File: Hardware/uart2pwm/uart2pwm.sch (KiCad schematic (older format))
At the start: 43 parts, among them IC1 ATTINY2313A-S, P1 CONN_01X04, P10 LED5, P11 CONN_01X03, P2 CONN_02X03, P3 LED0, P4 LED3, P5 FAN0, P6 LED1, P7 LED4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

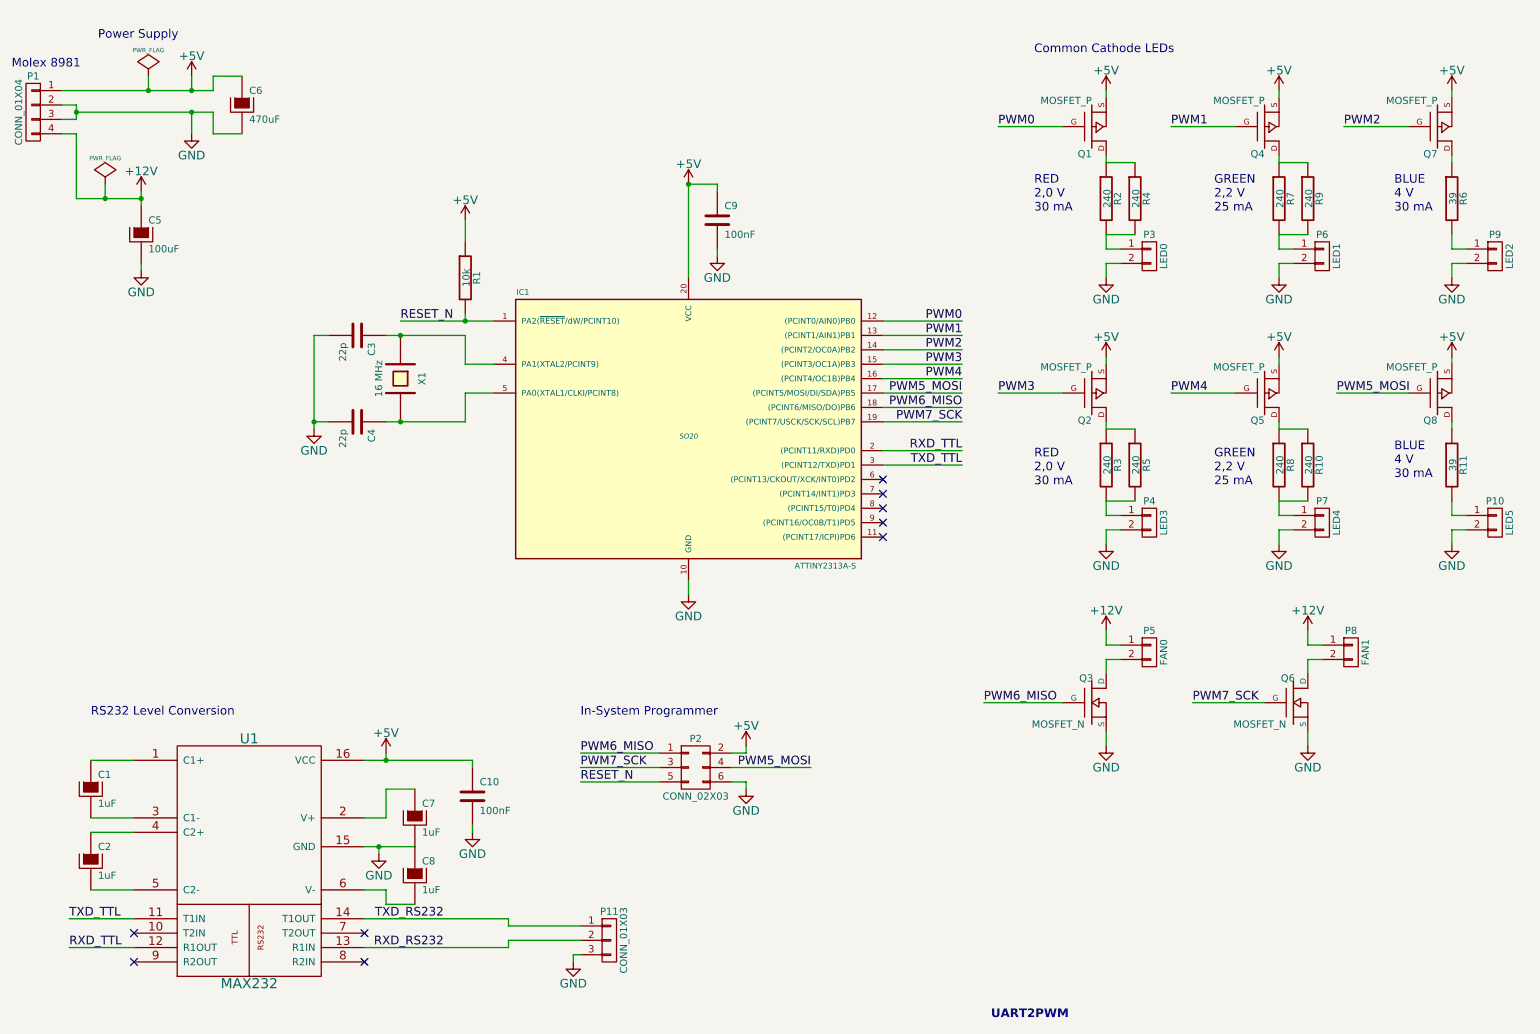
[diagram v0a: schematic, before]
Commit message: Schematic complete; Placement started
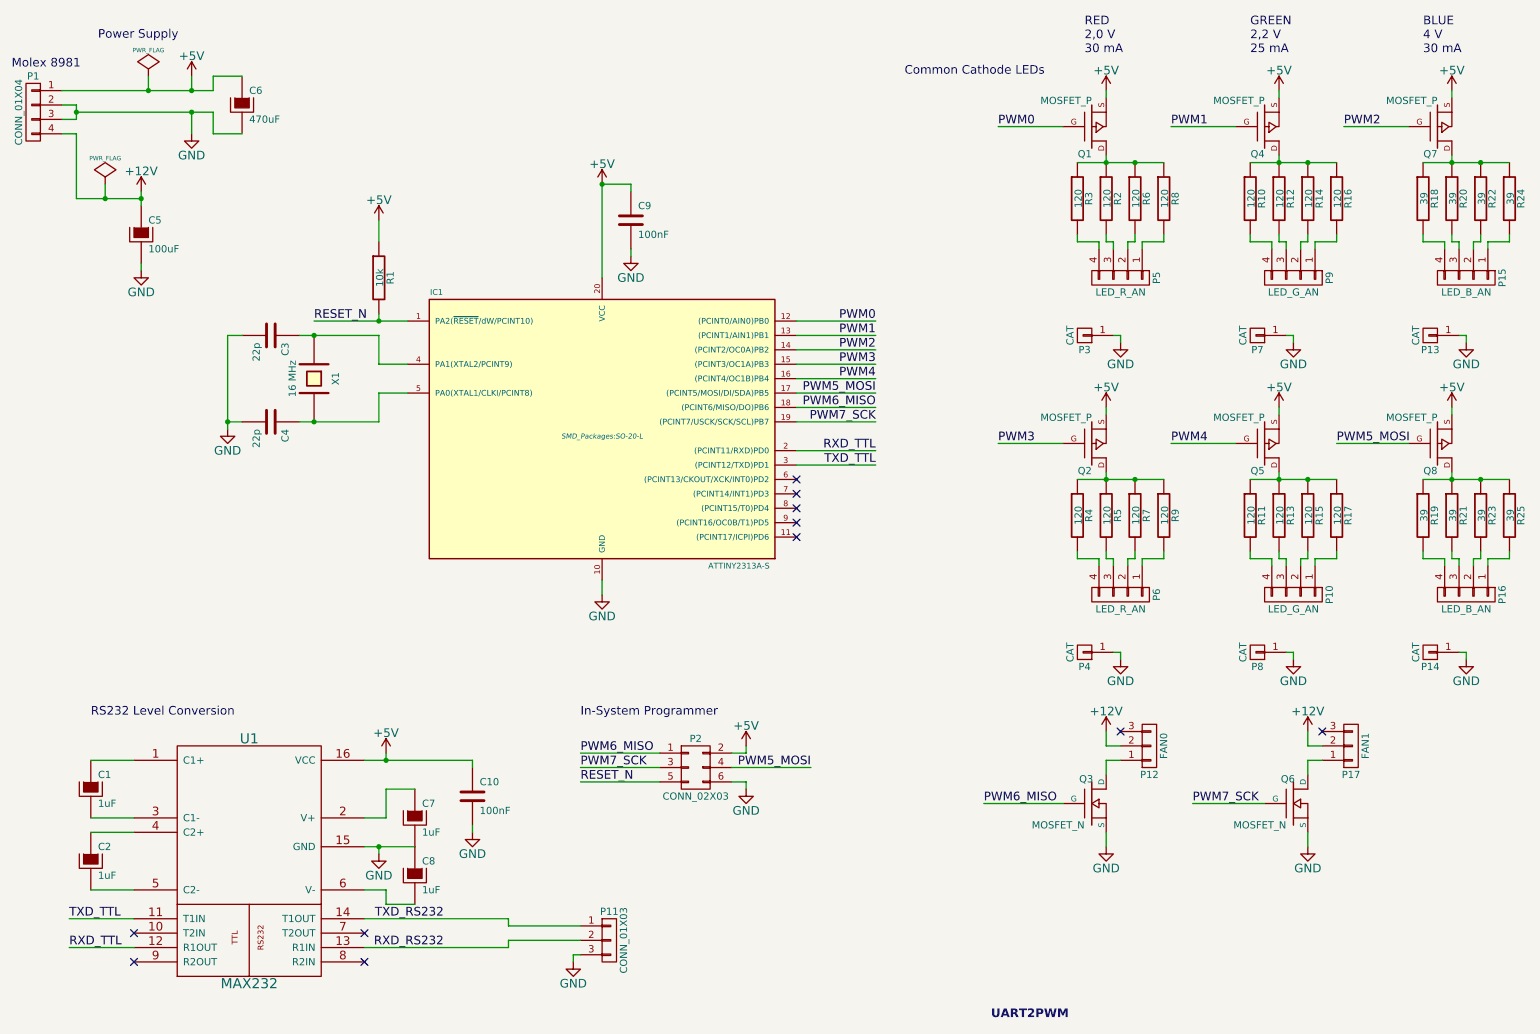
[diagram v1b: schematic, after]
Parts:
- removed P10: LED5, symbol CONN_01X02
- removed P3: LED0, symbol CONN_01X02
- removed P4: LED3, symbol CONN_01X02
- removed P5: FAN0, symbol CONN_01X02
- removed P6: LED1, symbol CONN_01X02
- removed P7: LED4, symbol CONN_01X02
- removed P8: FAN1, symbol CONN_01X02
- removed P9: LED2, symbol CONN_01X02
- added P10, P9: LED_G_AN, Pin_Headers:Pin_Header_Straight_2x02, symbol CONN_01X04
- added P12: FAN0, Pin_Headers:Pin_Header_Straight_1x03, symbol CONN_01X03
- added P13, P14, P3, P4, P7, P8: CAT, Pin_Headers:Pin_Header_Straight_1x01, symbol CONN_01X01
- added P15, P16: LED_B_AN, Pin_Headers:Pin_Header_Straight_2x02, symbol CONN_01X04
- added P17: FAN1, Pin_Headers:Pin_Header_Straight_1x03, symbol CONN_01X03
- added P5, P6: LED_R_AN, Pin_Headers:Pin_Header_Straight_2x02, symbol CONN_01X04
- added R12, R13, R14, R15, R16, R17: 120, SMD_Packages:SMD-0603, symbol R
- added R18, R19, R20, R21, R22, R23, R24, R25: 39, SMD_Packages:SMD-0603, symbol R
- C1, C2, C7, C8: footprint (none) -> Discret:C1V5
- C10, C3, C4, C9, R1: footprint (none) -> SMD_Packages:SMD-0603
- C5: footprint (none) -> Capacitors_Elko_ThroughHole:Elko_vert_11.5x8mm_RM3.5
- C6: footprint (none) -> Capacitors_Elko_ThroughHole:Elko_vert_20x10mm_RM5
- IC1: footprint SO20 -> SMD_Packages:SO-20-L
- P1: footprint (none) -> Connector:MOLEX_8981_4Pin
- P11: footprint (none) -> Pin_Headers:Pin_Header_Straight_1x03
- P2: footprint (none) -> Pin_Headers:Pin_Header_Straight_2x03
- Q1, Q2, Q3, Q4, Q5, Q6, Q7, Q8: footprint (none) -> SMD_Packages:SOT-23-GDS
- R10, R2, R3, R4, R5, R7, R8, R9: value 240 -> 120; footprint (none) -> SMD_Packages:SMD-0603
- R11, R6: value 39 -> 120; footprint (none) -> SMD_Packages:SMD-0603
- U1: footprint (none) -> Sockets_DIP:DIP-16__300
- X1: footprint (none) -> Crystals:Crystal_HC49-SD_SMD
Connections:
- net +12V: now also P12.2 (P2), P17.2 (P2)
- net GND: now also P13.1 (P1), P14.1 (P1), P3.1 (P1), P4.1 (P1), P7.1 (P1), P8.1 (P1)
- net at Q1.D, R2.1: now also R3.1, R6.1, R8.1; no longer R4.1
- net at R2.2: now also P5.3 (P3); no longer R4.2
- net at R7.1, R9.1: now also Q2.D, R4.1, R5.1; no longer Q4.D
- net at R7.2: now also P6.2 (P2); no longer R9.2
- net at Q7.D: now also R18.1, R20.1, R22.1, R24.1; no longer R6.1
- net at R6.2: now also P5.2 (P2)
- net at R3.2: now also P5.4 (P4); no longer R5.2
- net at R8.2: now also P5.1 (P1); no longer R10.2
- net at R11.1: now also Q5.D, R13.1, R15.1, R17.1; no longer Q8.D
- net at R11.2: now also P10.4 (P4)
- net at Q3.D: now also P12.1 (P1)
- net at Q6.D: now also P17.1 (P1)
- new net: Q4.D, R10.1, R12.1, R14.1, R16.1
- new net: Q8.D, R19.1, R21.1, R23.1, R25.1
- new net: P9.3 (P3), R12.2
- new net: P9.2 (P2), R14.2
- new net: P9.4 (P4), R10.2
- new net: P9.1 (P1), R16.2
- new net: P15.4 (P4), R18.2
- new net: P15.3 (P3), R20.2
- new net: P15.2 (P2), R22.2
- new net: P15.1 (P1), R24.2
- new net: P6.3 (P3), R5.2
- new net: P6.4 (P4), R4.2
- new net: P6.1 (P1), R9.2
- new net: P10.3 (P3), R13.2
- new net: P10.2 (P2), R15.2
- new net: P10.1 (P1), R17.2
- new net: P16.4 (P4), R19.2
- new net: P16.3 (P3), R21.2
- new net: P16.2 (P2), R23.2
- new net: P16.1 (P1), R25.2
- no-connect marks 9 -> 11
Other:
- moved on the sheet: C3, C4, C9, IC1, Q2, Q3, Q5, Q6, Q8, R1, X1

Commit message: Finalized first hardware revision
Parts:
- C1, C2, C7, C8: footprint Discret:C1V5 -> Capacitors_SMD:C_0805
- C6: footprint Capacitors_Elko_ThroughHole:Elko_vert_20x10mm_RM5 -> Capacitors_Elko_ThroughHole:Elko_vert_11.5x8mm_RM3.5
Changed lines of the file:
@@
 F 0 "C6" H 2200 1250 50  0000 L CNN
 F 1 "470uF" H 2200 1050 50  0000 L CNN
-F 2 "Capacitors_Elko_ThroughHole:Elko_vert_20x10mm_RM5" H 2250 1000 30  0001 C CNN
+F 2 "Capacitors_Elko_ThroughHole:Elko_vert_11.5x8mm_RM3.5" H 2250 1000 30  0001 C CNN
 F 3 "" H 2150 1150 300 0000 C CNN
 	1    2150 1150
@@
 F 0 "C1" H 1150 6000 50  0000 L CNN
 F 1 "1uF" H 1150 5800 50  0000 L CNN
-F 2 "Discret:C1V5" H 1200 5750 30  0001 C CNN
+F 2 "Capacitors_SMD:C_0805" H 1200 5750 30  0001 C CNN
 F 3 "" H 1100 5900 300 0000 C CNN
 	1    1100 5900
@@
 F 0 "C2" H 1150 6500 50  0000 L CNN
 F 1 "1uF" H 1150 6300 50  0000 L CNN
-F 2 "Discret:C1V5" H 1200 6250 30  0001 C CNN
+F 2 "Capacitors_SMD:C_0805" H 1200 6250 30  0001 C CNN
 F 3 "" H 1100 6400 300 0000 C CNN
 	1    1100 6400
@@
 F 0 "C7" H 3400 6200 50  0000 L CNN
 F 1 "1uF" H 3400 6000 50  0000 L CNN
-F 2 "Discret:C1V5" H 3450 5950 30  0001 C CNN
+F 2 "Capacitors_SMD:C_0805" H 3450 5950 30  0001 C CNN
 F 3 "" H 3350 6100 300 0000 C CNN
 	1    3350 6100
@@
 F 0 "C8" H 3400 6600 50  0000 L CNN
 F 1 "1uF" H 3400 6400 50  0000 L CNN
-F 2 "Discret:C1V5" H 3450 6350 30  0001 C CNN
+F 2 "Capacitors_SMD:C_0805" H 3450 6350 30  0001 C CNN
 F 3 "" H 3350 6500 300 0000 C CNN
 	1    3350 6500
